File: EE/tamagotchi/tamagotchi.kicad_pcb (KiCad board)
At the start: 4 copper layers, 43.5 x 38.8 mm, 48 parts, among them J1 Conn_01x02_Male, J3 Conn_01x07, J7 TAG_CONNECT, J8 Conn_01x02_Male, P1 USB_C_Plug_USB2.0, Q1 Q_NMOS_GSD, Q2 Q_NMOS_GSD, Q4 Q_NMOS_GSD, Q5 Q_PMOS_GSD, SW2 TL1260BQRBLK, U2 STM32G031G8Ux, U3 MPL3115A2

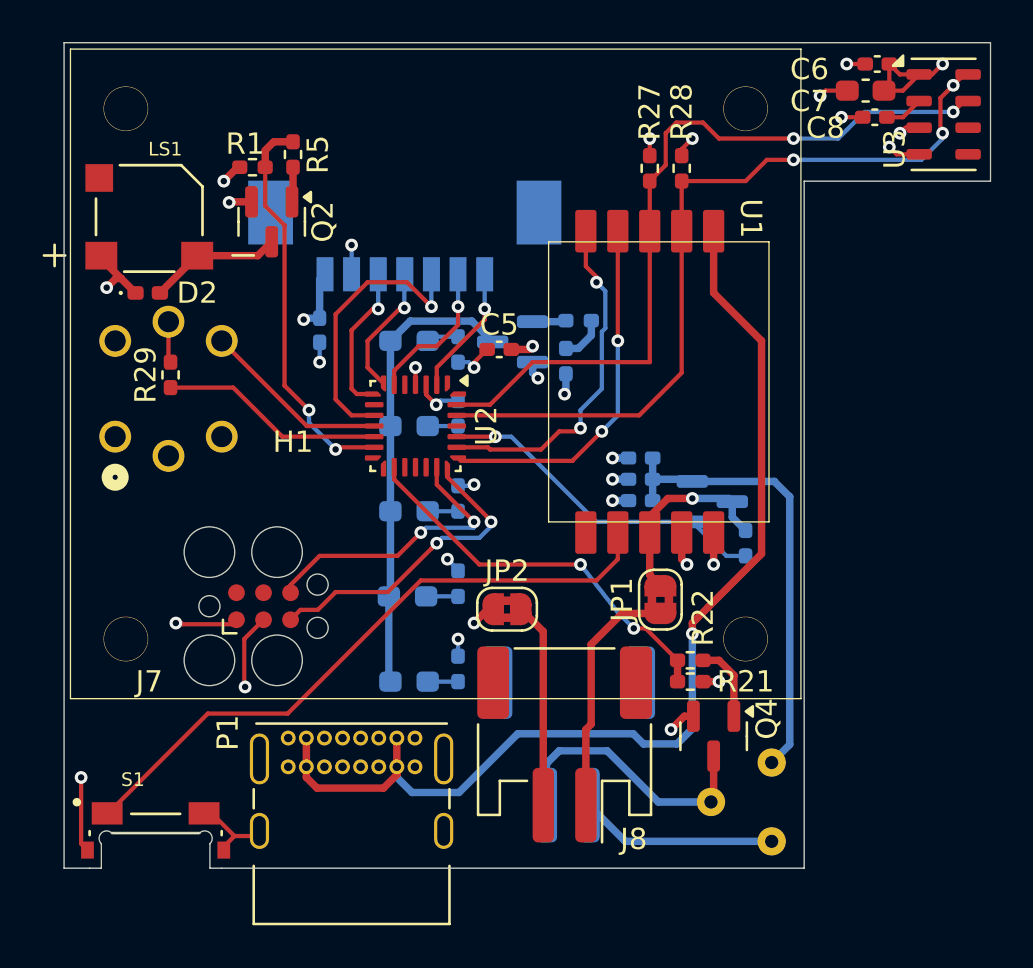
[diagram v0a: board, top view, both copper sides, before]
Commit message: WIP - Overall Cleanup, Power Change
Added expected loads for power in schematic.
Changed power arch to use existing design that appears to work.
Removed rear backlight LEDs - shouldn't be necessary.
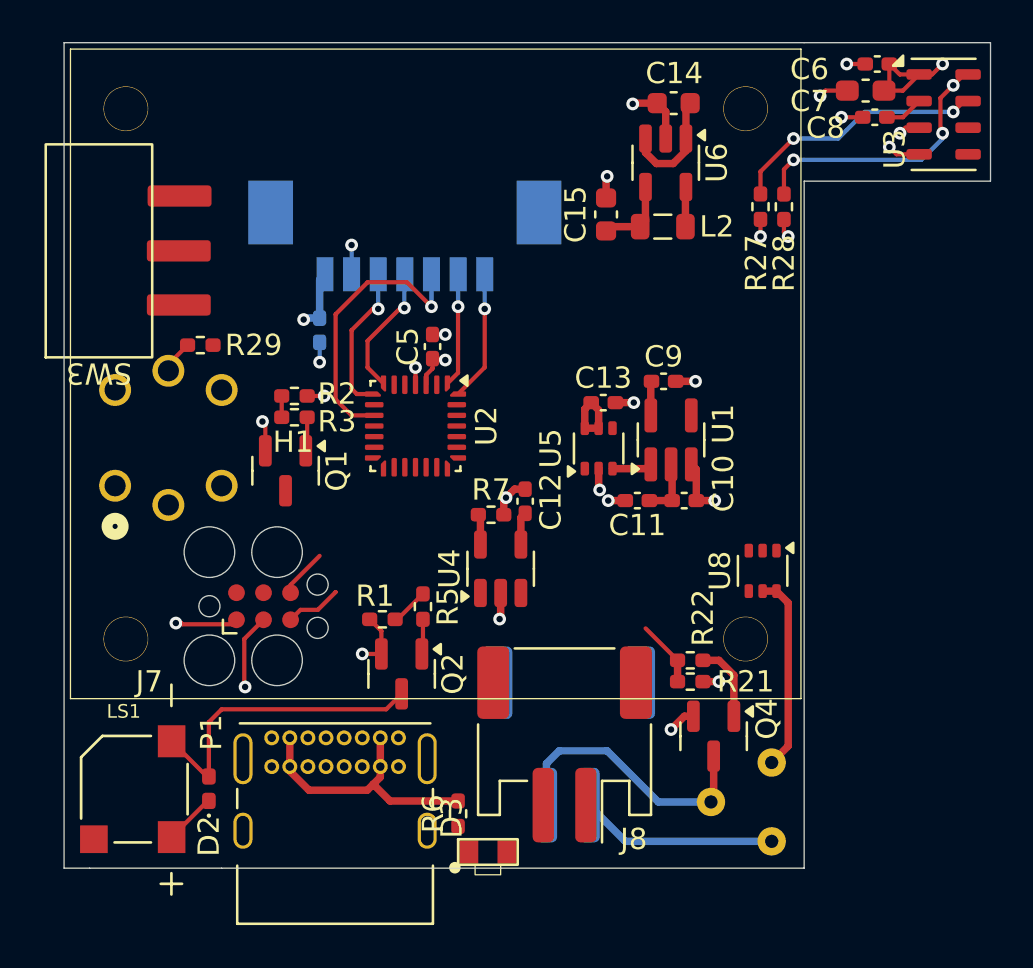
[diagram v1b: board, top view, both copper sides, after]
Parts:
- removed C2: 1u, Capacitor_SMD:C_0402_1005Metric_Pad0.74x0.62mm_HandSolder
- removed C3: 4.7u, Capacitor_SMD:C_0402_1005Metric_Pad0.74x0.62mm_HandSolder
- removed C4: 0.1u, Capacitor_SMD:C_0402_1005Metric_Pad0.74x0.62mm_HandSolder
- removed D1, D6, D7, D8, D9: LED, LED_SMD:LED_0603_1608Metric_Pad1.05x0.95mm_HandSolder
- removed JP1, JP2: SolderJumper_2_Bridged, Jumper:SolderJumper-2_P1.3mm_Bridged2Bar_RoundedPad1.0x1.5mm
- removed Q5: Q_PMOS_GSD, Package_TO_SOT_SMD:SOT-23
- removed R14, R15, R16, R17: R, Resistor_SMD:R_0402_1005Metric_Pad0.72x0.64mm_HandSolder
- removed R23: 100k, Resistor_SMD:R_0402_1005Metric_Pad0.72x0.64mm_HandSolder
- removed R4: 33, Resistor_SMD:R_0402_1005Metric_Pad0.72x0.64mm_HandSolder
- removed S1: EVQ-P4HB3B, Library:SW_EVQ-P4HB3B
- added C10: 1u, Capacitor_SMD:C_0402_1005Metric_Pad0.74x0.62mm_HandSolder, F.Cu at (165.1, 92.5)
- added C11: 0.1u, Capacitor_SMD:C_0402_1005Metric_Pad0.74x0.62mm_HandSolder, F.Cu at (162.9, 92.5)
- added C12: 1u, Capacitor_SMD:C_0402_1005Metric_Pad0.74x0.62mm_HandSolder, F.Cu at (157.7, 92.5)
- added C13: 1u, Capacitor_SMD:C_0402_1005Metric_Pad0.74x0.62mm_HandSolder, F.Cu at (161.3, 87.9)
- added C14: 4.7u, Capacitor_SMD:C_0603_1608Metric, F.Cu at (164.6, 73.8)
- added C15: 4.7u, Capacitor_SMD:C_0603_1608Metric, F.Cu at (161.4, 79.1)
- added C9: 1u, Capacitor_SMD:C_0402_1005Metric_Pad0.74x0.62mm_HandSolder, F.Cu at (164.2, 86.9)
- added D3: LED, Library:LED_0604, F.Cu at (155.0, 109.0)
- added L2: 4.7u, Inductor_SMD:L_0805_2012Metric, F.Cu at (164.1, 79.6)
- added R6: 3.3k, Resistor_SMD:R_0402_1005Metric_Pad0.72x0.64mm_HandSolder, F.Cu at (154.5, 107.2)
- added R7: 3.3k, Resistor_SMD:R_0402_1005Metric_Pad0.72x0.64mm_HandSolder, F.Cu at (156.0, 93.2)
- added SW3: SW_SPDT_321, Library:EGJ1210, F.Cu at (141.4, 80.8)
- added U4: STC4054GR, Package_TO_SOT_SMD:TSOT-23-5, F.Cu at (156.5, 95.7)
- added U5: TPS22919QDCKRQ1, Package_TO_SOT_SMD:SOT-363_SC-70-6, F.Cu at (161.1, 90.1)
- added U6: LM3670MF-3.3/NOPB, Package_TO_SOT_SMD:TSOT-23-5, F.Cu at (164.2, 76.6)
- added U8: TPS22919QDCKRQ1, Package_TO_SOT_SMD:SOT-363_SC-70-6, F.Cu at (168.8, 95.8)
- Q1: moved to F.Cu
- R2: value R -> 10k; moved to F.Cu
- R29: value 2.2k -> 1k
- R3: value 100k -> 33; moved to F.Cu
- U1: value ~ -> TPS3840PL30DBVR; footprint Library:BatteryBoard -> Package_TO_SOT_SMD:SC-74A-5_1.55x2.9mm_P0.95mm
- moved LS1 26.8 mm to (139.3, 106.0), turned to 90 degrees
- moved D2 23.5 mm to (142.8, 106.0), turned to 90 degrees
- moved Q2 22.1 mm to (151.8, 100.6)
- moved R1 22.1 mm to (150.9, 98.1)
- moved R5 22.1 mm to (152.8, 97.5)
- moved R2 14.9 mm to (146.8, 87.6), turned to 0 degrees
- moved R3 13.0 mm to (146.8, 88.6), turned to 0 degrees
- moved Q1 12.3 mm to (146.4, 91.1), turned to -90 degrees
- moved R27 5.50 mm to (168.7, 78.7), turned to 90 degrees
- moved U1 5.30 mm to (164.5, 89.7), turned to 90 degrees
- moved R28 5.13 mm to (169.8, 78.7), turned to 90 degrees
- moved C5 3.14 mm to (153.3, 85.3), turned to 90 degrees
- moved SW2 2.31 mm to (138.4, 91.8)
- moved R29 1.98 mm to (142.4, 85.2), turned to 180 degrees
- moved P1 0.78 mm to (145.8, 103.6)
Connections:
- J8 pad 1: Net-(J8-Pin_1) -> /Power/VBAT_PRESWITCH
- J8 pad 2: Net-(J8-Pin_2) -> GND
- Q1 pad 3: Net-(D1-K) -> Net-(Q1-D)
- R2 pad 1: +3V3 -> /MCU/VAPE_LED
- R2 pad 2: Net-(D1-A) -> GND
- R29 pad 1: /MCU/VAPE_LED -> +3V3
- R3 pad 1: /Display/VAPE_EN -> /MCU/VAPE_LED
- R3 pad 2: GND -> Net-(Q1-G)
- SW2 pad 5: GND -> Net-(Q1-D)
- U1 pad 1: VBUS -> /Power/MONITOR
- U1 pad 2: /SCL -> /Power/VBAT
- U1 pad 3: /SDA -> GND
- U1 pad 4: /MCU/INT_N -> unconnected-(U1-MR_N-Pad4)
- U1 pad 5: /MCU/CE_N -> /Power/CT
- U2 pad 1: unconnected-(U2-PC14-Pad1) -> /Display/DC
- U2 pad 2: /Display/RST -> unconnected-(U2-PC15-Pad2)
- U2 pad 22: /MCU/INT_N -> unconnected-(U2-PA15-Pad22)
- U2 pad 23: /MCU/CE_N -> unconnected-(U2-PB3-Pad23)
- U2 pad 28: unconnected-(U2-PB8-Pad28) -> /Display/RST
- U2 pad 6: /Display/DC -> unconnected-(U2-PA0-Pad6)
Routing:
- net VBUS: track 50.2 -> 14.1 mm, vias 1 -> 0
- net /Power/SWITCH: track 30.2 -> 0.00 mm
- net /SCL: track 37.2 -> 12.9 mm
- net /SDA: track 36.4 -> 12.2 mm
- net Net-(D1-K): track 21.7 -> 0.00 mm
- net /MCU/INT_N: track 17.1 -> 0.00 mm, vias 2 -> 0
- net /Display/BUZZ_PWM: track 18.7 -> 1.80 mm, vias 2 -> 0
- net /MCU/CE_N: track 16.4 -> 0.00 mm, vias 2 -> 0
- net /MCU/VAPE_EN_N: track 15.9 -> 0.00 mm, vias 1 -> 0
- net /MCU/VAPE_PWM: track 18.6 -> 3.12 mm, vias 2 -> 0
- net /Vape/VBAT_CONT: track 21.6 -> 9.35 mm
- net /MCU/SWCLK: track 14.8 -> 2.65 mm, vias 2 -> 0
- net Net-(J8-Pin_1): track 11.5 -> 0.00 mm
- net /MCU/SWDIO: track 13.6 -> 2.29 mm, vias 2 -> 0
- net Net-(J8-Pin_2): track 9.63 -> 0.00 mm
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
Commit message: Pre Error check, layoutcomplete
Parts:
- D3: moved to B.Cu
- moved R6 35.3 mm to (141.8, 74.3), turned to 0 degrees
- moved D3 33.1 mm to (136.4, 81.6), turned to 90 degrees
- moved U4 21.7 mm to (146.3, 76.5), turned to 0 degrees
- moved R7 18.6 mm to (148.8, 76.0), turned to -90 degrees
- moved C12 17.0 mm to (149.5, 77.7), turned to 0 degrees
- moved U5 11.1 mm to (158.8, 79.2)
- moved C10 11.1 mm to (162.9, 81.6)
- moved C11 11.1 mm to (160.7, 81.6)
- moved C13 11.1 mm to (159.1, 77.0)
- moved C9 11.1 mm to (161.9, 76.0)
- moved U1 11.1 mm to (162.2, 78.8)
- moved C15 11.0 mm to (161.6, 90.0)
- moved L2 11.0 mm to (164.2, 90.6)
- moved U6 11.0 mm to (164.4, 87.6)
- moved C14 11.0 mm to (164.7, 84.8)
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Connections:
- U2 pad 11: /MCU/VAPE_SW -> /MCU/VAPE_LED
- U2 pad 12: /MCU/VAPE_LED -> /MCU/VAPE_SW
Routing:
- net /Power/VBAT_PRESWITCH: track 0.00 -> 60.5 mm, vias 0 -> 2
- net VBUS: track 14.1 -> 68.1 mm, vias 0 -> 1
- net /VBAT: track 8.66 -> 37.0 mm
- net /Power/VBAT: track 2.79 -> 26.2 mm
- net /SCL: track 12.9 -> 34.0 mm, vias 3 -> 5
- net /SDA: track 12.2 -> 31.7 mm, vias 2 -> 4
- net /MCU/VAPE_EN_N: track 0.00 -> 15.9 mm
- net /MCU/VAPE_PWM: track 3.12 -> 18.3 mm, vias 0 -> 2
- net Net-(D3-K): track 0.00 -> 13.2 mm, vias 0 -> 1
- net /MCU/VAPE_SW: track 0.00 -> 11.3 mm
- net /Display/BUZZ_PWM: track 1.80 -> 10.5 mm
- net /MCU/SWCLK: track 2.65 -> 10.8 mm, vias 0 -> 2
- net Net-(D3-A): track 0.00 -> 7.66 mm, vias 0 -> 1
- net /MCU/SWDIO: track 2.29 -> 9.78 mm, vias 0 -> 2
- net +3V3: track 23.4 -> 29.5 mm, vias 7 -> 12
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
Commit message: Minor Updates
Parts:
- moved R6 0.30 mm to (142.1, 74.3)
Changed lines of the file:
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@@
 	(footprint "Resistor_SMD:R_0402_1005Metric_Pad0.72x0.64mm_HandSolder"
 		(layer "F.Cu")
-		(at 141.7975 74.3)
+		(at 142.1 74.3)
 		(descr "Resistor SMD 0402 (1005 Metric), square (rectangular) end terminal, IPC-7351 nominal with elongated pad for handsoldering. (Body size source: IPC-SM-782 page 72, https://www.pcb-3d.com/wordpress/wp-content/uploads/ipc-sm-782a_amendment_1_and_2.pdf), generated with kicad-footprint-generator")
 		(tags "resistor handsolder")
@@
 		(tags "resistor handsolder")
 		(property "Reference" "R3"
-			(at 1.9975 0.2 0)
+			(at 2.0825 -0.1875 90)
 			(layer "F.SilkS")
 			(effects
@@
 		(at 136.3 71.3)
 		(property "Reference" "H1"
-			(at 10.45 18.45 0)
+			(at 1 0.8 0)
 			(unlocked yes)
 			(layer "F.SilkS")
@@
 		(tags "resistor handsolder")
 		(property "Reference" "R29"
-			(at -2.5025 0 0)
+			(at -2.5025 0.5 0)
 			(layer "F.SilkS")
 			(effects
@@
 		(tags "resistor handsolder")
 		(property "Reference" "R2"
-			(at 1.9975 -0.1 0)
+			(at -0.017501 -1 0)
 			(layer "F.SilkS")
 			(effects
@@
 		(at 141.387124 80.773785 90)
 		(property "Reference" "SW3"
-			(at -5.75 -3.749999 180)
+			(at -1.326215 0.312876 0)
 			(unlocked yes)
 			(layer "F.SilkS")
@@
 	)
 	(segment
-		(start 142.395 74.3)
-		(end 140.595 72.5)
+		(start 142.1 102.5)
+		(end 137.3 102.5)
 		(width 0.35)
 		(layer "F.Cu")
@@
 	)
 	(segment
-		(start 137.3 102.5)
-		(end 142.1 102.5)
+		(start 136.7199 74.1801)
+		(end 138.4 72.5)
 		(width 0.35)
 		(layer "F.Cu")
@@
 	)
 	(segment
-		(start 145.9 74.3)
-		(end 142.395 74.3)
+		(start 140.8975 72.5)
+		(end 142.6975 74.3)
 		(width 0.35)
 		(layer "F.Cu")
@@
 	)
 	(segment
-		(start 136.7199 101.9199)
-		(end 137.3 102.5)
-		(width 0.35)
-		(layer "F.Cu")
-		(net 10)
-	)
-	(segment
-		(start 138.4 72.5)
-		(end 136.7199 74.1801)
+		(start 148.702498 77.449999)
+		(end 148.9025 77.650001)
 		(width 0.35)
 		(layer "F.Cu")
@@
 	)
 	(segment
-		(start 148.702498 77.449999)
-		(end 148.9025 77.650001)
+		(start 147.4375 77.449999)
+		(end 148.702498 77.449999)
 		(width 0.35)
 		(layer "F.Cu")
@@
 	)
 	(segment
-		(start 147.4375 77.449999)
-		(end 148.702498 77.449999)
+		(start 137.3 102.5)
+		(end 136.7199 101.9199)
 		(width 0.35)
 		(layer "F.Cu")
@@
 	)
 	(segment
-		(start 136.7199 74.1801)
-		(end 136.7199 101.9199)
+		(start 145.9 74.3)
+		(end 142.6975 74.3)
 		(width 0.35)
 		(layer "F.Cu")
@@
 	)
 	(segment
-		(start 140.595 72.5)
-		(end 138.4 72.5)
+		(start 136.7199 101.9199)
+		(end 136.7199 74.1801)
 		(width 0.35)
 		(layer "F.Cu")
@@
 	)
 	(segment
+		(start 138.4 72.5)
+		(end 140.8975 72.5)
+		(width 0.35)
+		(layer "F.Cu")
+		(net 10)
+	)
+	(segment
 		(start 146.201 74.601)
 		(end 145.9 74.3)
@@
 	)
 	(segment
-		(start 140.759734 74.3)
-		(end 137.4 77.659734)
+		(start 137.4 77.659734)
+		(end 140.759734 74.3)
 		(width 0.2)
 		(layer "F.Cu")
@@
 	)
 	(segment
-		(start 137.4 77.659734)
-		(end 137.4 78.4)
+		(start 137.4 78.4)
+		(end 137.4 77.659734)
 		(width 0.2)
 		(layer "F.Cu")
@@
 	)
 	(segment
-		(start 141.2 74.3)
-		(end 140.759734 74.3)
+		(start 140.759734 74.3)
+		(end 141.5025 74.3)
 		(width 0.2)
 		(layer "F.Cu")
